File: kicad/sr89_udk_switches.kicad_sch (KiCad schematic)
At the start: 139 parts

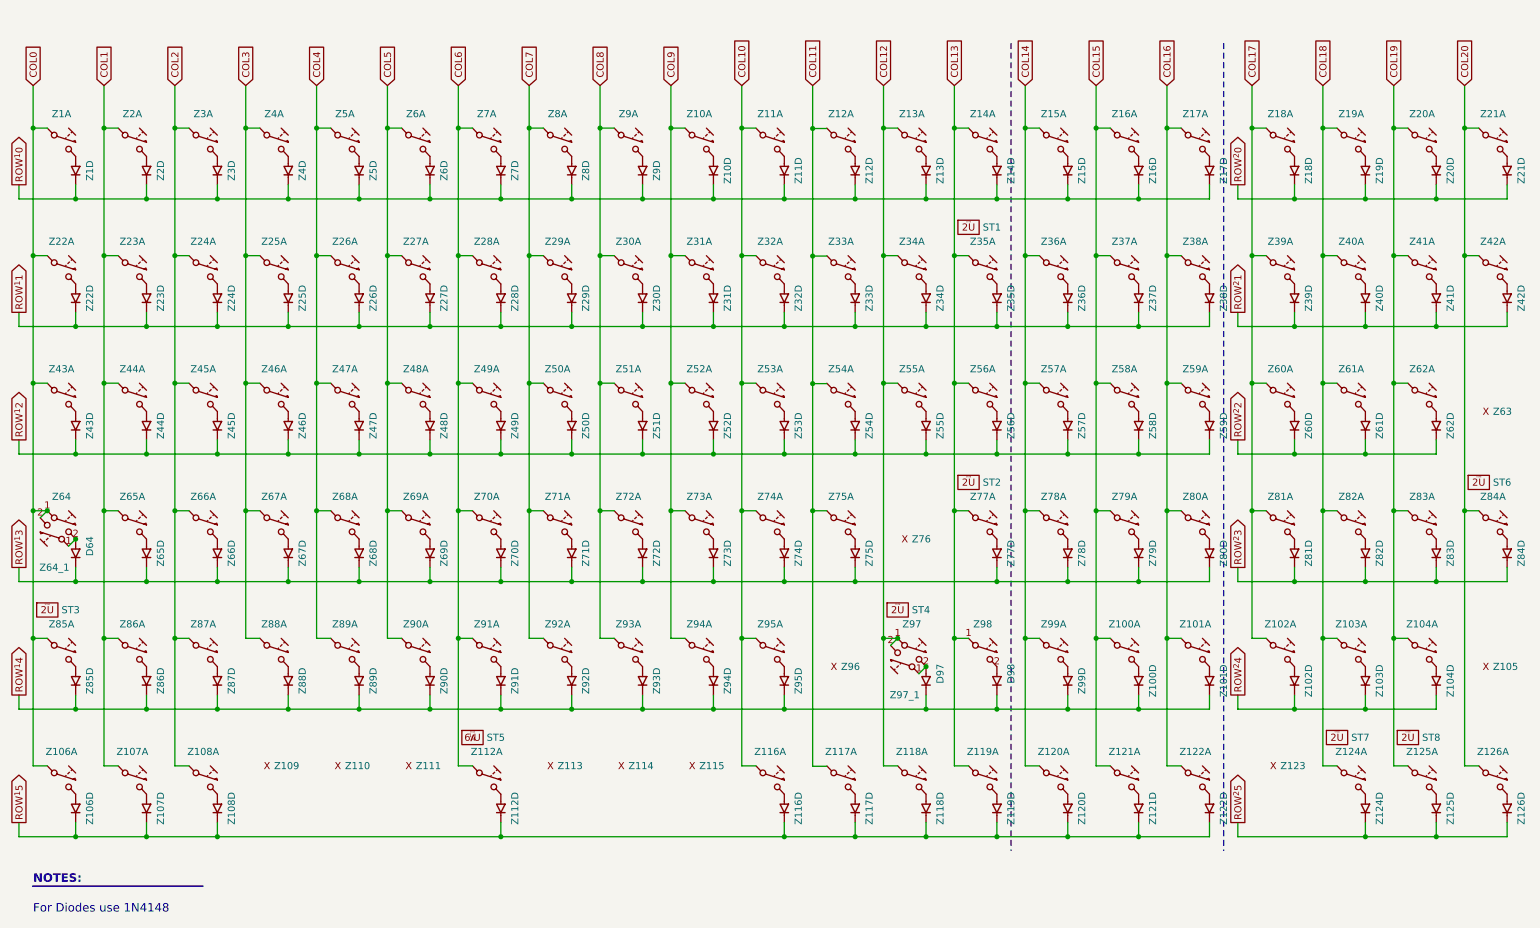
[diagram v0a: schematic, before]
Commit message: routed, but not rules checked
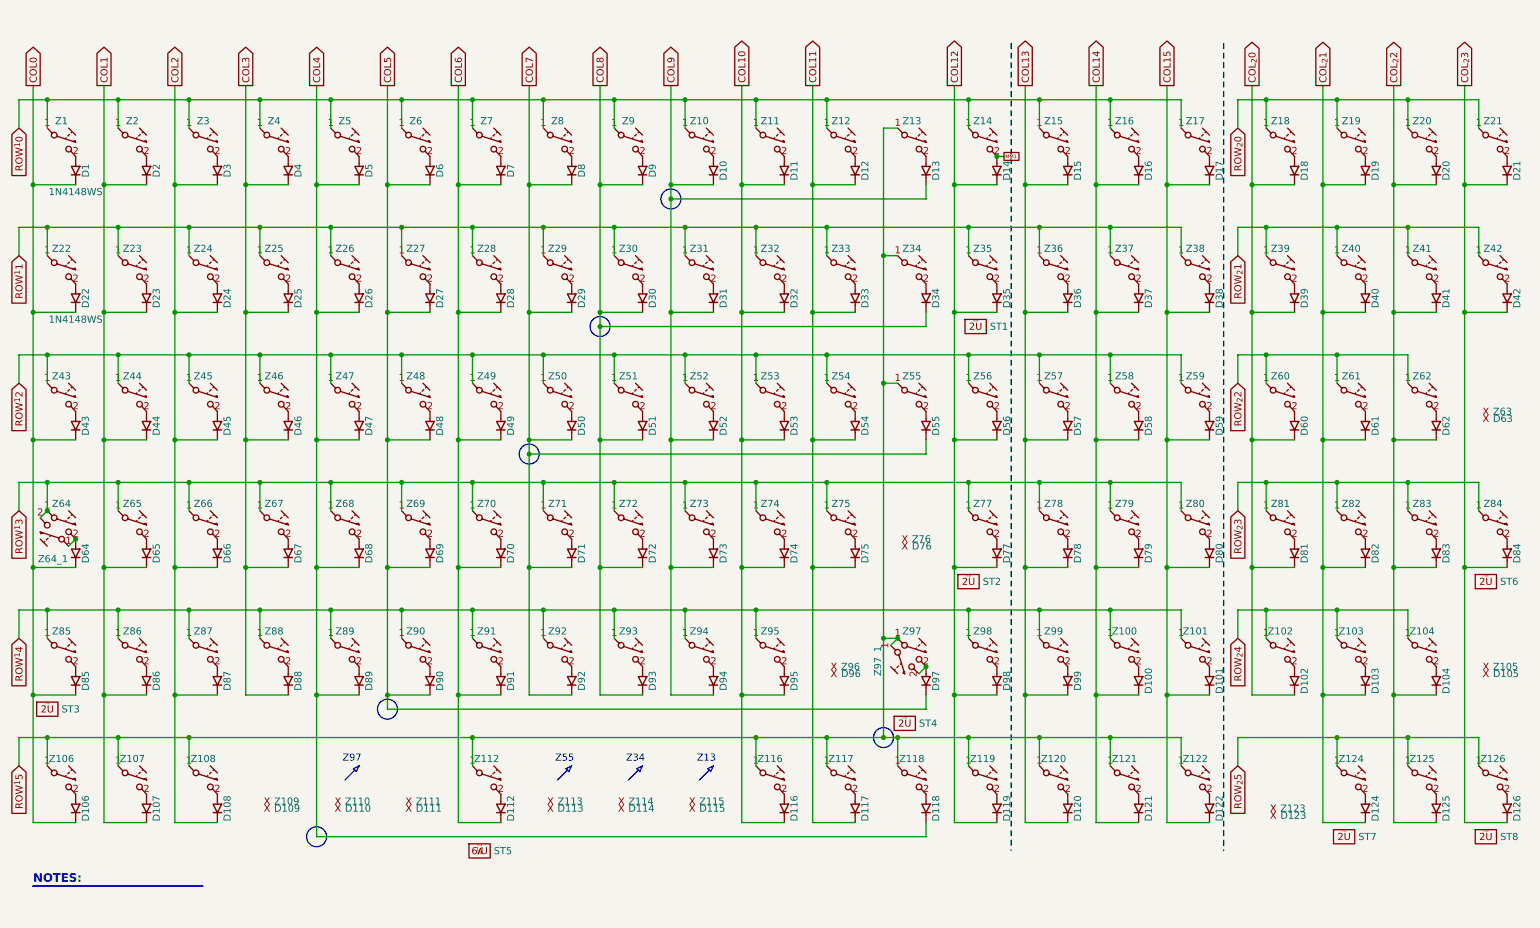
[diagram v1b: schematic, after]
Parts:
- removed Z1, Z10, Z100, Z101, Z102, Z103, Z104, Z11, Z12, Z126, Z13, Z14, Z15, Z16, Z17, Z18, Z19, Z2, Z20, Z21, Z3, Z4, Z43, Z44, Z45, Z46, Z47, Z48, Z49, Z5, Z50, Z51, Z52, Z53, Z54, Z55, Z56, Z57, Z58, Z59, Z6, Z60, Z61, Z62, Z7, Z8, Z84, Z85, Z86, Z87, Z88, Z89, Z9, Z90, Z91, Z92, Z93, Z94, Z95, Z99: (no value), 0_sr89:Combined_SW_1, symbol 0_sr89:Combined_SW
- removed Z106, Z107, Z108, Z112, Z116, Z117, Z118, Z119, Z120, Z121, Z122, Z124, Z125, Z22, Z23, Z24, Z25, Z26, Z27, Z28, Z29, Z30, Z31, Z32, Z33, Z34, Z35, Z36, Z37, Z38, Z39, Z40, Z41, Z42, Z65, Z66, Z67, Z68, Z69, Z70, Z71, Z72, Z73, Z74, Z75, Z77, Z78, Z79, Z80, Z81, Z82, Z83: (no value), 0_sr89:Combined_SW_2, symbol 0_sr89:Combined_SW
- added D1, D10, D100, D101, D102, D103, D104, D106, D107, D108, D11, D112, D116, D117, D118, D119, D12, D120, D121, D122, D124, D125, D126, D13, D14, D15, D16, D17, D18, D19, D2, D20, D21, D22, D23, D24, D25, D26, D27, D28, D29, D3, D30, D31, D32, D33, D34, D35, D36, D37, D38, D39, D4, D40, D41, D42, D43, D44, D45, D46, D47, D48, D49, D5, D50, D51, D52, D53, D54, D55, D56, D57, D58, D59, D6, D60, D61, D62, D65, D66, D67, D68, D69, D7, D70, D71, D72, D73, D74, D75, D77, D78, D79, D8, D80, D81, D82, D83, D84, D85, D86, D87, D88, D89, D9, D90, D91, D92, D93, D94, D95, D99: 1N4148WS, ts-keyboard-lib:D_SOD-323, symbol ts-kicad-lib:D
- added D105, D109, D110, D111, D113, D114, D115, D123, D63, D76, D96: (no value), symbol 0_sr89:X
- added Z1, Z10, Z100, Z101, Z102, Z103, Z104, Z106, Z107, Z108, Z11, Z112, Z116, Z117, Z118, Z119, Z12, Z120, Z121, Z122, Z124, Z125, Z126, Z13, Z14, Z15, Z16, Z17, Z18, Z19, Z2, Z20, Z21, Z22, Z23, Z24, Z25, Z26, Z27, Z28, Z29, Z3, Z30, Z31, Z32, Z33, Z34, Z35, Z36, Z37, Z38, Z39, Z4, Z40, Z41, Z42, Z43, Z44, Z45, Z46, Z47, Z48, Z49, Z5, Z50, Z51, Z52, Z53, Z54, Z55, Z56, Z57, Z58, Z59, Z6, Z60, Z61, Z62, Z65, Z66, Z67, Z68, Z69, Z7, Z70, Z71, Z72, Z73, Z74, Z75, Z77, Z78, Z79, Z8, Z80, Z81, Z82, Z83, Z84, Z85, Z86, Z87, Z88, Z89, Z9, Z90, Z91, Z92, Z93, Z94, Z95, Z99: (no value), ts-keyboard-lib:SW_MX_HotSwap, symbol ts-keyboard-lib:SW_SPST_45
- D64, D97, D98: value 1N4148 -> 1N4148WS; footprint (none) -> ts-keyboard-lib:D_SOD-323; LCSC (none) -> C2128
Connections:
- net COL0: now also D64.1 (K), D1.1 (K), D106.1 (K), D22.1 (K), D43.1 (K), D85.1 (K); no longer Z64.1, Z64_1.2
- net COL1: now also D107.1 (K), D2.1 (K), D23.1 (K), D44.1 (K), D65.1 (K), D86.1 (K)
- net COL10: now also D11.1 (K), D116.1 (K), D32.1 (K), D53.1 (K), D74.1 (K), D95.1 (K)
- net COL11: now also D117.1 (K), D12.1 (K), D33.1 (K), D54.1 (K), D75.1 (K)
- net COL12: now also D98.1 (K), D119.1 (K), D14.1 (K), D35.1 (K), D56.1 (K), D77.1 (K); no longer Z97.1, Z97_1.2
- net COL13: now also D120.1 (K), D15.1 (K), D36.1 (K), D57.1 (K), D78.1 (K), D99.1 (K); no longer Z98.1
- net COL14: now also D100.1 (K), D121.1 (K), D16.1 (K), D37.1 (K), D58.1 (K), D79.1 (K)
- net COL15: now also D101.1 (K), D122.1 (K), D17.1 (K), D38.1 (K), D59.1 (K), D80.1 (K)
- net COL2: now also D108.1 (K), D24.1 (K), D3.1 (K), D45.1 (K), D66.1 (K), D87.1 (K)
- net COL3: now also D25.1 (K), D4.1 (K), D46.1 (K), D67.1 (K), D88.1 (K)
- net COL4: now also D118.1 (K), D26.1 (K), D47.1 (K), D5.1 (K), D68.1 (K), D89.1 (K)
- net COL5: now also D97.1 (K), D27.1 (K), D48.1 (K), D6.1 (K), D69.1 (K), D90.1 (K)
- net COL6: now also D112.1 (K), D28.1 (K), D49.1 (K), D7.1 (K), D70.1 (K), D91.1 (K)
- net COL7: now also D29.1 (K), D50.1 (K), D55.1 (K), D71.1 (K), D8.1 (K), D92.1 (K)
- net COL8: now also D30.1 (K), D34.1 (K), D51.1 (K), D72.1 (K), D9.1 (K), D93.1 (K)
- net COL9: now also D10.1 (K), D13.1 (K), D31.1 (K), D52.1 (K), D73.1 (K), D94.1 (K)
- net ROW^{1}0: now also Z1.1, Z10.1, Z11.1, Z12.1, Z14.1, Z15.1, Z16.1, Z17.1, Z2.1, Z3.1, Z4.1, Z5.1, Z6.1, Z7.1, Z8.1, Z9.1
- net ROW^{1}1: now also Z22.1, Z23.1, Z24.1, Z25.1, Z26.1, Z27.1, Z28.1, Z29.1, Z30.1, Z31.1, Z32.1, Z33.1, Z35.1, Z36.1, Z37.1, Z38.1
- net ROW^{1}2: now also Z43.1, Z44.1, Z45.1, Z46.1, Z47.1, Z48.1, Z49.1, Z50.1, Z51.1, Z52.1, Z53.1, Z54.1, Z56.1, Z57.1, Z58.1, Z59.1
- net ROW^{1}3: now also Z64.1, Z64_1.2, Z65.1, Z66.1, Z67.1, Z68.1, Z69.1, Z70.1, Z71.1, Z72.1, Z73.1, Z74.1, Z75.1, Z77.1, Z78.1, Z79.1, Z80.1; no longer D64.1 (K)
- net ROW^{1}4: now also Z98.1, Z100.1, Z101.1, Z85.1, Z86.1, Z87.1, Z88.1, Z89.1, Z90.1, Z91.1, Z92.1, Z93.1, Z94.1, Z95.1, Z99.1; no longer D97.1 (K), D98.1 (K)
- net ROW^{1}5: now also Z97.1, Z97_1.1, Z106.1, Z107.1, Z108.1, Z112.1, Z116.1, Z117.1, Z118.1, Z119.1, Z120.1, Z121.1, Z122.1, Z13.1, Z34.1, Z55.1
- net at D97.2 (A), Z97.2: now also Z97_1.2; no longer Z97_1.1
- new net: D112.2 (A), Z112.2
- new net: D57.2 (A), Z57.2
- new net: D87.2 (A), Z87.2
- new net: D101.2 (A), Z101.2
- new net: D116.2 (A), Z116.2
- new net: D17.2 (A), Z17.2
- new net: D86.2 (A), Z86.2
- new net: D106.2 (A), Z106.2
- new net: D1.2 (A), Z1.2
- new net: D21.2 (A), Z21.2
- new net: D52.2 (A), Z52.2
- new net: D73.2 (A), Z73.2
- new net: D19.2 (A), Z19.2
- new net: D28.2 (A), Z28.2
- new net: D31.2 (A), Z31.2
- new net: D29.2 (A), Z29.2
- new net: D85.2 (A), Z85.2
- new net: D117.2 (A), Z117.2
- new net: D104.2 (A), Z104.2
- new net: D68.2 (A), Z68.2
- new net: D44.2 (A), Z44.2
- new net: D34.2 (A), Z34.2
- new net: D69.2 (A), Z69.2
- new net: D84.2 (A), Z84.2
- new net: D33.2 (A), Z33.2
- new net: D39.2 (A), Z39.2
- new net: D51.2 (A), Z51.2
- new net: D95.2 (A), Z95.2
- new net: D20.2 (A), Z20.2
- new net: D120.2 (A), Z120.2
- new net: D61.2 (A), Z61.2
- new net: D94.2 (A), Z94.2
- new net: D4.2 (A), Z4.2
- new net: D100.2 (A), Z100.2
- new net: D7.2 (A), Z7.2
- new net: D49.2 (A), Z49.2
- new net: D90.2 (A), Z90.2
- new net: D8.2 (A), Z8.2
- new net: D27.2 (A), Z27.2
- new net: D48.2 (A), Z48.2
- new net: D92.2 (A), Z92.2
- new net: D72.2 (A), Z72.2
- new net: D37.2 (A), Z37.2
- new net: D10.2 (A), Z10.2
- new net: D77.2 (A), Z77.2
- new net: D24.2 (A), Z24.2
- new net: D59.2 (A), Z59.2
- new net: D83.2 (A), Z83.2
- new net: D122.2 (A), Z122.2
- new net: D62.2 (A), Z62.2
- new net: D103.2 (A), Z103.2
- new net: D81.2 (A), Z81.2
- new net: D3.2 (A), Z3.2
- new net: D2.2 (A), Z2.2
- new net: D99.2 (A), Z99.2
- new net: D75.2 (A), Z75.2
- new net: D36.2 (A), Z36.2
- new net: D23.2 (A), Z23.2
- new net: D118.2 (A), Z118.2
- new net: D119.2 (A), Z119.2
- new net: D65.2 (A), Z65.2
- new net: D40.2 (A), Z40.2
- new net: D102.2 (A), Z102.2
- new net: D93.2 (A), Z93.2
- new net: D12.2 (A), Z12.2
- new net: D79.2 (A), Z79.2
- new net: D91.2 (A), Z91.2
- new net: D11.2 (A), Z11.2
- new net: D80.2 (A), Z80.2
- new net: D70.2 (A), Z70.2
- new net: D66.2 (A), Z66.2
- new net: D38.2 (A), Z38.2
- new net: D78.2 (A), Z78.2
- new net: D9.2 (A), Z9.2
- new net: D46.2 (A), Z46.2
- new net: D6.2 (A), Z6.2
- new net: D107.2 (A), Z107.2
- new net: D55.2 (A), Z55.2
- new net: D88.2 (A), Z88.2
- new net: D121.2 (A), Z121.2
- new net: D16.2 (A), Z16.2
- new net: D15.2 (A), Z15.2
- new net: D71.2 (A), Z71.2
- new net: D56.2 (A), Z56.2
- new net: D43.2 (A), Z43.2
- new net: D30.2 (A), Z30.2
- new net: D5.2 (A), Z5.2
- new net: D35.2 (A), Z35.2
- new net: D50.2 (A), Z50.2
- new net: D126.2 (A), Z126.2
- new net: D60.2 (A), Z60.2
- new net: D32.2 (A), Z32.2
- new net: D82.2 (A), Z82.2
- new net: D54.2 (A), Z54.2
- new net: D58.2 (A), Z58.2
- new net: D13.2 (A), Z13.2
- new net: D45.2 (A), Z45.2
- new net: D18.2 (A), Z18.2
- new net: D41.2 (A), Z41.2
- new net: D53.2 (A), Z53.2
- new net: D42.2 (A), Z42.2
- new net: D26.2 (A), Z26.2
- new net: D108.2 (A), Z108.2
- new net: D124.2 (A), Z124.2
- new net: D22.2 (A), Z22.2
- new net: D89.2 (A), Z89.2
- new net: D125.2 (A), Z125.2
- new net: D47.2 (A), Z47.2
- new net: D74.2 (A), Z74.2
- new net: D25.2 (A), Z25.2
- new net: D67.2 (A), Z67.2
- new net COL_{2}0: D102.1 (K), D18.1 (K), D39.1 (K), D60.1 (K), D81.1 (K)
- new net COL_{2}1: D103.1 (K), D124.1 (K), D19.1 (K), D40.1 (K), D61.1 (K), D82.1 (K)
- new net COL_{2}2: D104.1 (K), D125.1 (K), D20.1 (K), D41.1 (K), D62.1 (K), D83.1 (K)
- new net COL_{2}3: D126.1 (K), D21.1 (K), D42.1 (K), D84.1 (K)
- new net MM1: D14.2 (A), Z14.2
- new net ROW_{2}0: Z18.1, Z19.1, Z20.1, Z21.1
- new net ROW_{2}1: Z39.1, Z40.1, Z41.1, Z42.1
- new net ROW_{2}2: Z60.1, Z61.1, Z62.1
- new net ROW_{2}3: Z81.1, Z82.1, Z83.1, Z84.1
- new net ROW_{2}4: Z102.1, Z103.1, Z104.1
- new net ROW_{2}5: Z124.1, Z125.1, Z126.1
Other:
- note added: "Z13"
- note added: "Z34"
- note added: "Z55"
- note added: "Z97"
- note removed: "For Diodes use 1N4148"
- moved on the sheet: ST1, ST2, ST3, ST4, ST5, ST6, ST7, ST8, Z109, Z110, Z111, Z113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
